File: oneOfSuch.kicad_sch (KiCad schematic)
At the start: 5 parts, among them J1 Reset Button, J2 Boot Button, U1 esp32-s3-wroom-1

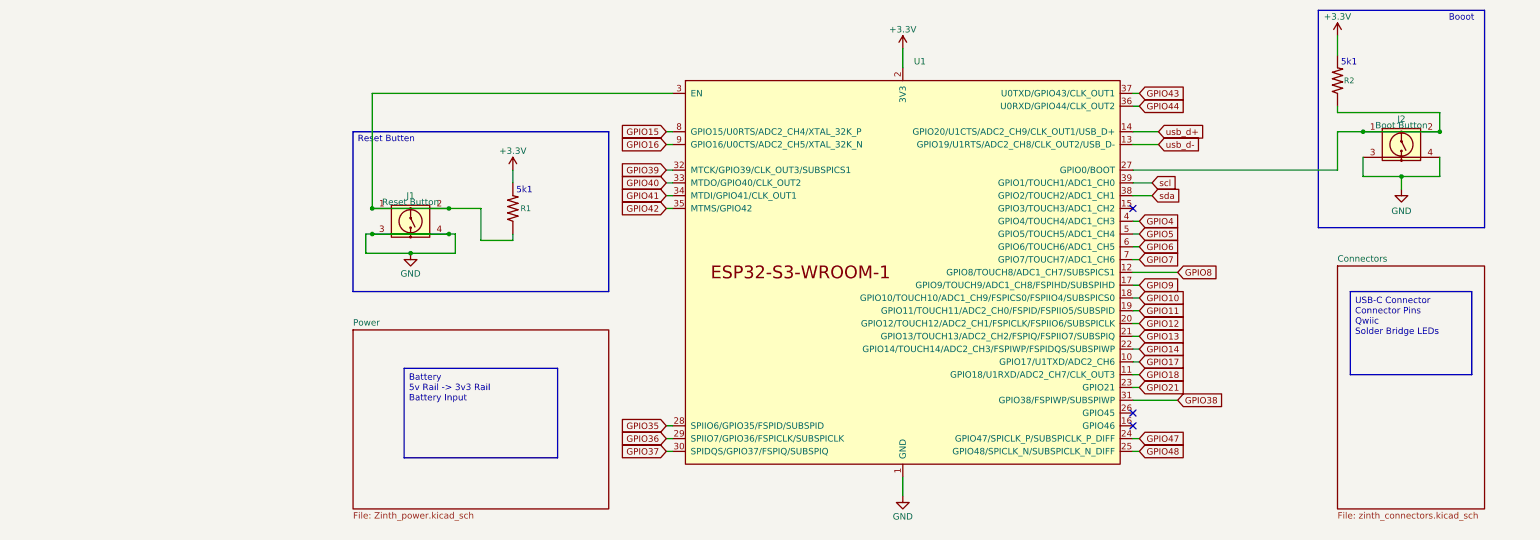
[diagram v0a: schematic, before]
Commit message: added some stuff to schematic and PCB design
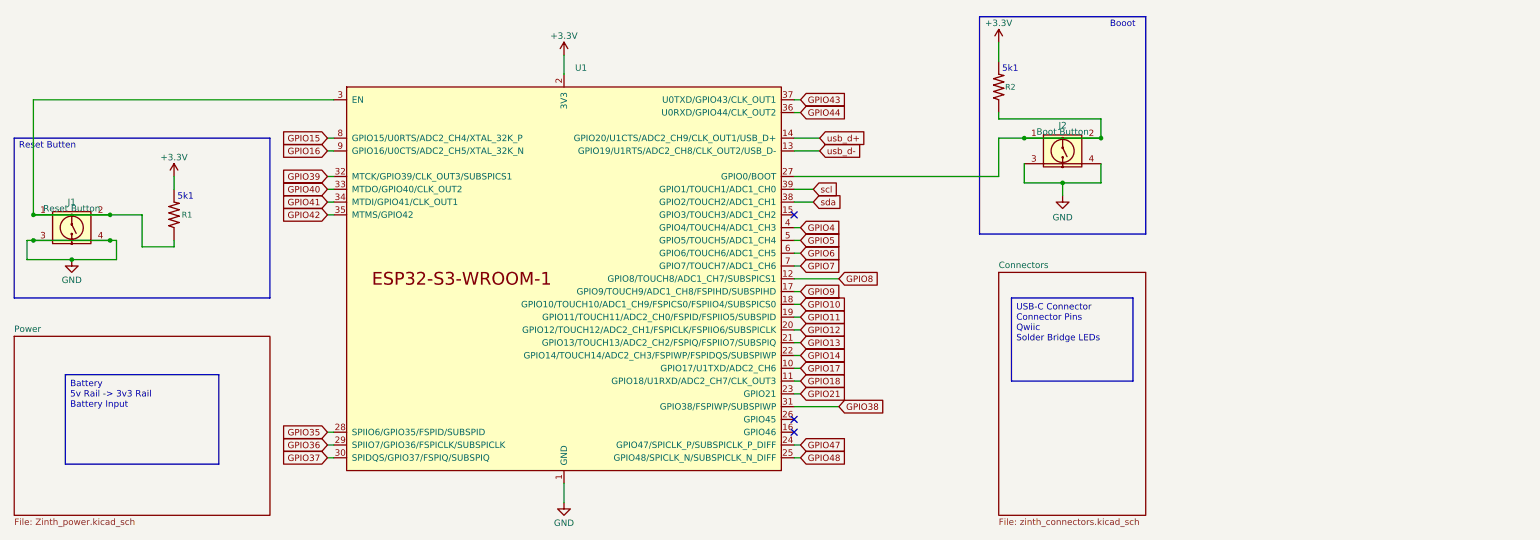
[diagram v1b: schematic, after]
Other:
- moved on the sheet: J1, J2, R1, R2, U1
